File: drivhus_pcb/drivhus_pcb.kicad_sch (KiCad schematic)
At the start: 13 parts, among them J1 Setup, J10 RS-485 Right Bus, J2 Conn_01x19_Female, J3 Conn_01x19_Female, J4 RS-485 Left Bus, J5 Conn_Coaxial_Power, J6 +12V, J7 -12V, J8 +5V, J9 -5V, U1 SP3485EN

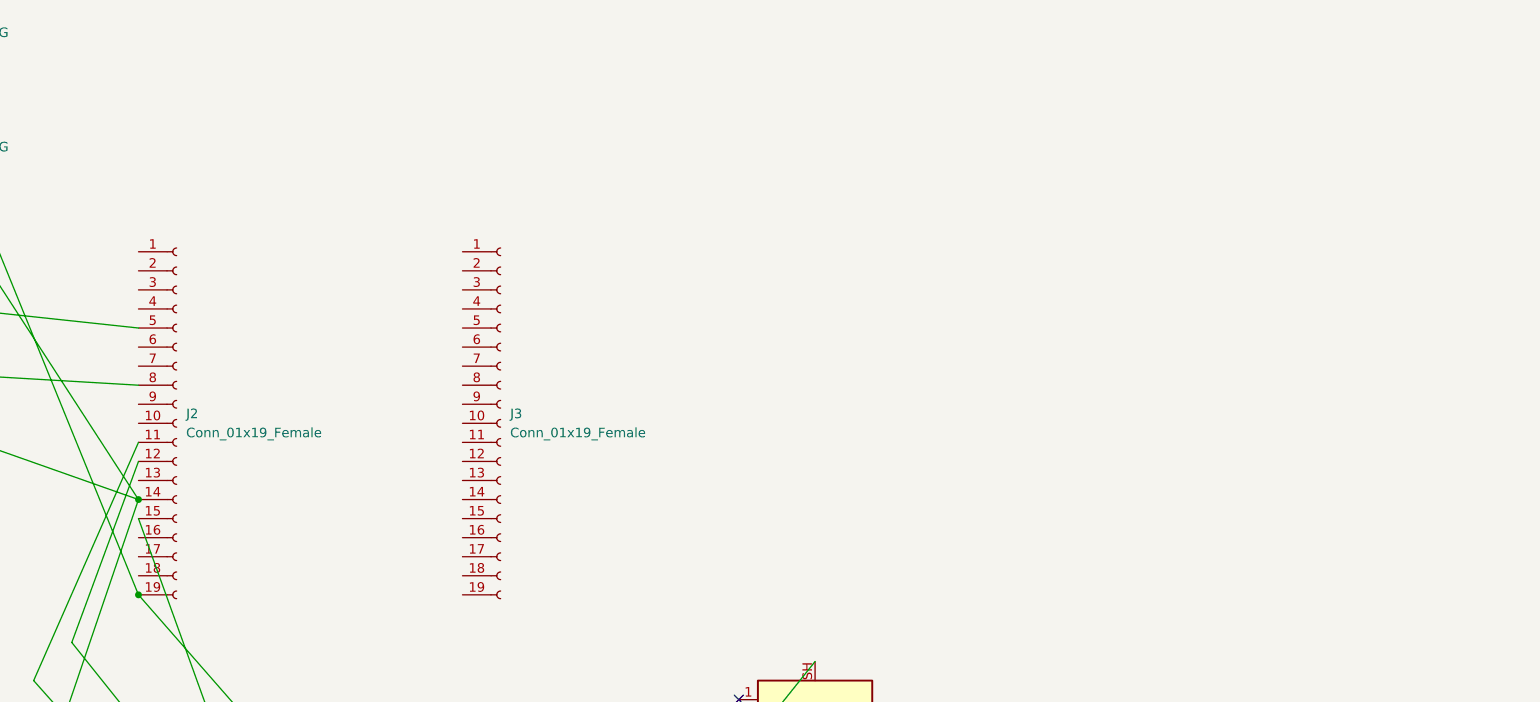
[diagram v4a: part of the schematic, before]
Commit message: Added connectors for indoor and outdoor temp/humid/light sensors
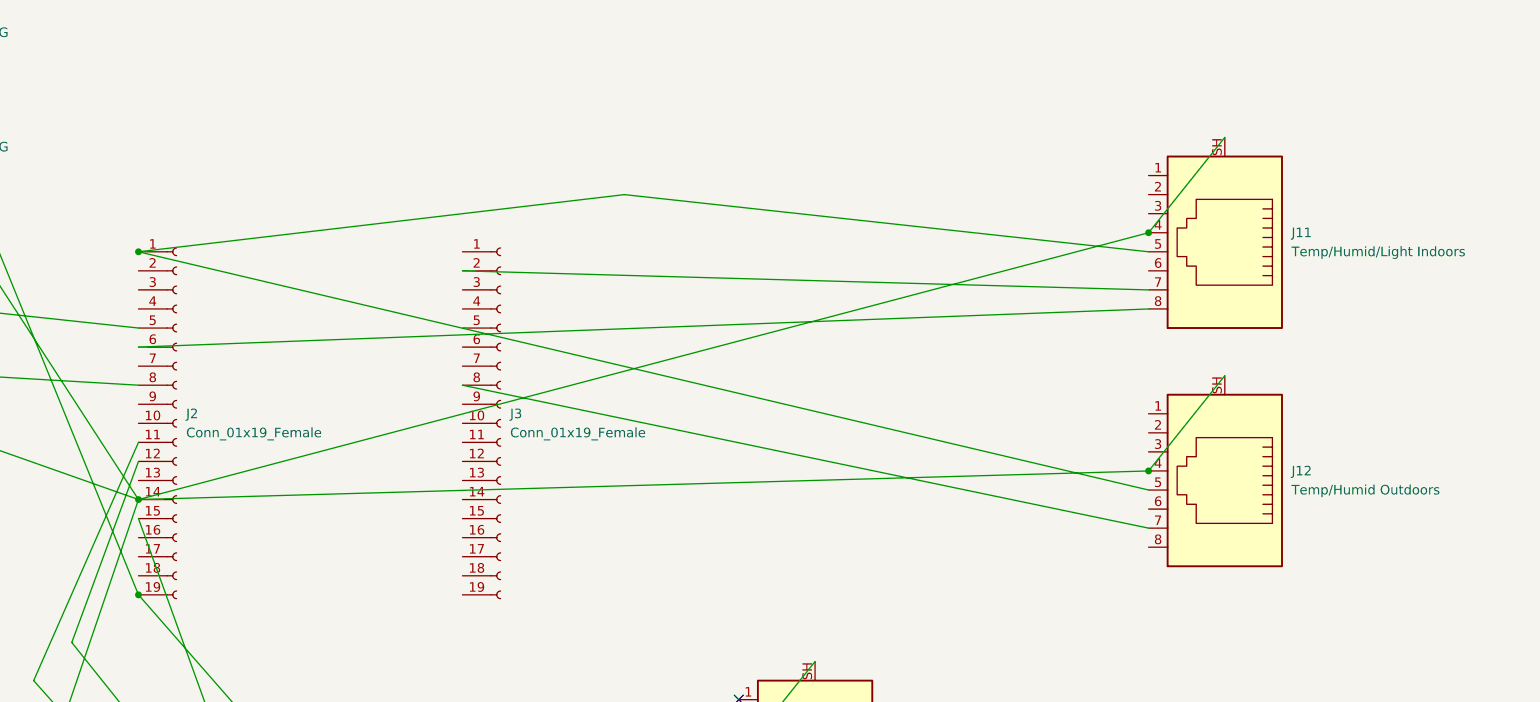
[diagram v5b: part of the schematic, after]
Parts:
- added J11: Temp/Humid/Light Indoors, Connector_RJ:RJ45_Ninigi_GE, symbol Connector:RJ45_Shielded
- added J12: Temp/Humid Outdoors, Connector_RJ:RJ45_Ninigi_GE, symbol Connector:RJ45_Shielded
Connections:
- net GND: now also J11.4, J11.SH, J12.4, J12.SH
- net at J2.1 (Pin_1): now also J11.5, J12.5
- net at J2.6 (Pin_6): now also J11.8
- net at J3.2 (Pin_2): now also J11.7
- net at J3.8 (Pin_8): now also J12.7
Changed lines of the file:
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@@
   (junction (at 99.06 107.95) (diameter 0) (color 0 0 0 0)
   )
+  (junction (at 233.68 91.44) (diameter 0) (color 0 0 0 0)
+  )
   (junction (at 27.94 64.77) (diameter 0) (color 0 0 0 0)
   )
+  (junction (at 99.06 62.23) (diameter 0) (color 0 0 0 0)
+  )
   (junction (at 135.89 146.05) (diameter 0) (color 0 0 0 0)
+  )
+  (junction (at 233.68 59.69) (diameter 0) (color 0 0 0 0)
   )
   (junction (at 68.58 33.02) (diameter 0) (color 0 0 0 0)
@@
     (stroke (width 0) (type default) (color 0 0 0 0))
   )
+  (wire (pts (xy 99.06 95.25) (xy 233.68 91.44))
+    (stroke (width 0) (type default) (color 0 0 0 0))
+  )
+  (wire (pts (xy 163.83 54.61) (xy 233.68 62.23))
+    (stroke (width 0) (type default) (color 0 0 0 0))
+  )
+  (wire (pts (xy 99.06 74.93) (xy 233.68 69.85))
+    (stroke (width 0) (type default) (color 0 0 0 0))
+  )
   (wire (pts (xy 179.07 129.54) (xy 189.23 116.84))
     (stroke (width 0) (type default) (color 0 0 0 0))
@@
     (stroke (width 0) (type default) (color 0 0 0 0))
   )
+  (wire (pts (xy 99.06 62.23) (xy 163.83 54.61))
+    (stroke (width 0) (type default) (color 0 0 0 0))
+  )
   (wire (pts (xy 115.57 146.05) (xy 115.57 151.13))
     (stroke (width 0) (type default) (color 0 0 0 0))
@@
     (stroke (width 0) (type default) (color 0 0 0 0))
   )
+  (wire (pts (xy 233.68 59.69) (xy 243.84 46.99))
+    (stroke (width 0) (type default) (color 0 0 0 0))
+  )
+  (wire (pts (xy 233.68 91.44) (xy 243.84 78.74))
+    (stroke (width 0) (type default) (color 0 0 0 0))
+  )
   (wire (pts (xy 135.89 146.05) (xy 179.07 137.16))
     (stroke (width 0) (type default) (color 0 0 0 0))
@@
     (stroke (width 0) (type default) (color 0 0 0 0))
   )
+  (wire (pts (xy 142.24 80.01) (xy 233.68 99.06))
+    (stroke (width 0) (type default) (color 0 0 0 0))
+  )
+  (wire (pts (xy 99.06 95.25) (xy 233.68 59.69))
+    (stroke (width 0) (type default) (color 0 0 0 0))
+  )
   (wire (pts (xy 99.06 95.25) (xy 78.74 154.94))
     (stroke (width 0) (type default) (color 0 0 0 0))
@@
     (stroke (width 0) (type default) (color 0 0 0 0))
   )
+  (wire (pts (xy 99.06 62.23) (xy 233.68 93.98))
+    (stroke (width 0) (type default) (color 0 0 0 0))
+  )
   (wire (pts (xy 44.45 45.72) (xy 44.45 48.26))
     (stroke (width 0) (type default) (color 0 0 0 0))
@@
     (stroke (width 0) (type default) (color 0 0 0 0))
   )
+  (wire (pts (xy 142.24 64.77) (xy 233.68 67.31))
+    (stroke (width 0) (type default) (color 0 0 0 0))
+  )
   (wire (pts (xy 125.73 138.43) (xy 179.07 132.08))
     (stroke (width 0) (type default) (color 0 0 0 0))
@@
     )
     (pin "1")
+  )
+  (symbol (lib_id "Connector:RJ45_Shielded") (at 243.84 91.44 180) (unit 1)
+    (in_bom yes) (on_board yes) (fields_autoplaced)
+    (property "Reference" "J12" (id 0) (at 252.73 91.4399 0)
+      (effects (font (size 1.27 1.27)) (justify right))
+    )
+    (property "Value" "Temp/Humid Outdoors" (id 1) (at 252.73 93.9799 0)
+      (effects (font (size 1.27 1.27)) (justify right))
+    )
+    (property "Footprint" "Connector_RJ:RJ45_Ninigi_GE" (id 2) (at 243.84 92.075 90)
+      (effects (font (size 1.27 1.27)) hide)
+    )
+    (property "Datasheet" "~" (id 3) (at 243.84 92.075 90)
+      (effects (font (size 1.27 1.27)) hide)
+    )
+    (pin "1")
+    (pin "2")
+    (pin "3")
+    (pin "4")
+    (pin "5")
+    (pin "6")
+    (pin "7")
+    (pin "8")
+    (pin "SH")
   )
   (symbol (lib_id "Connector:Conn_01x19_Female") (at 104.14 85.09 0) (unit 1)
@@
     (pin "9")
   )
+  (symbol (lib_id "Connector:RJ45_Shielded") (at 243.84 59.69 180) (unit 1)
+    (in_bom yes) (on_board yes) (fields_autoplaced)
+    (property "Reference" "J11" (id 0) (at 252.73 59.6899 0)
+      (effects (font (size 1.27 1.27)) (justify right))
+    )
+    (property "Value" "Temp/Humid/Light Indoors" (id 1) (at 252.73 62.2299 0)
+      (effects (font (size 1.27 1.27)) (justify right))
+    )
+    (property "Footprint" "Connector_RJ:RJ45_Ninigi_GE" (id 2) (at 243.84 60.325 90)
+      (effects (font (size 1.27 1.27)) hide)
+    )
+    (property "Datasheet" "~" (id 3) (at 243.84 60.325 90)
+      (effects (font (size 1.27 1.27)) hide)
+    )
+    (pin "1")
+    (pin "2")
+    (pin "3")
+    (pin "4")
+    (pin "5")
+    (pin "6")
+    (pin "7")
+    (pin "8")
+    (pin "SH")
+  )
   (symbol (lib_id "power:+5V") (at 68.58 33.02 270) (unit 1)
     (in_bom yes) (on_board yes) (fields_autoplaced)
@@
       (reference "J10") (unit 1) (value "RS-485 Right Bus") (footprint "Connector_RJ:RJ45_Ninigi_GE")
     )
+    (path "/4c469707-9012-4c4e-9b88-e445c5c64803"
+      (reference "J11") (unit 1) (value "Temp/Humid/Light Indoors") (footprint "Connector_RJ:RJ45_Ninigi_GE")
+    )
+    (path "/1a8cb90e-f5bd-4cd7-b987-feae025c484b"
+      (reference "J12") (unit 1) (value "Temp/Humid Outdoors") (footprint "Connector_RJ:RJ45_Ninigi_GE")
+    )
     (path "/57442f99-2d46-4e71-bd92-43296b060c85"

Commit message: Added relays. Added lots and lots of relays...
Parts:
- added D1, D10, D11, D12, D13, D14, D15, D2, D3, D4, D5, D6, D7, D8, D9: D, Diode_SMD:D_SMB, symbol Device:D
- added J13, J14, J15, J16, J17, J18, J19, J20, J21, J22, J23, J24, J25, J26, J27: Conn_01x02_Male, TerminalBlock:TerminalBlock_bornier-2_P5.08mm, symbol Connector:Conn_01x02_Male
- added K1, K10, K11, K12, K13, K14, K15, K2, K3, K4, K5, K6, K7, K8, K9: SANYOU_SRD_Form_C, Relay_THT:Relay_SPDT_SANYOU_SRD_Series_Form_C, symbol Relay:SANYOU_SRD_Form_C
- added Q1, Q10, Q11, Q12, Q13, Q14, Q15, Q2, Q3, Q4, Q5, Q6, Q7, Q8, Q9: BC817, Package_TO_SOT_SMD:SOT-23, symbol Transistor_BJT:BC817
- added R10, R11, R12, R13, R14, R15, R16, R17, R3, R4, R5, R6, R7, R8, R9: 1K, Resistor_SMD:R_1206_3216Metric, symbol Device:R
- added U2: CD74HC4067M, Package_SO:SOIC-24W_7.5x15.4mm_P1.27mm, symbol 74xx:CD74HC4067M
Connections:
- net +5V: now also D1.1 (K), D10.1 (K), D11.1 (K), D12.1 (K), D13.1 (K), D14.1 (K), D15.1 (K), D2.1 (K), D3.1 (K), D4.1 (K), D5.1 (K), D6.1 (K), D7.1 (K), D8.1 (K), D9.1 (K), K1.5, K10.5, K11.5, K12.5, K13.5, K14.5, K15.5, K2.5, K3.5, K4.5, K5.5, K6.5, K7.5, K8.5, K9.5, U2.24 (VCC)
- net GND: now also Q1.2 (E), Q10.2 (E), Q11.2 (E), Q12.2 (E), Q13.2 (E), Q14.2 (E), Q15.2 (E), Q2.2 (E), Q3.2 (E), Q4.2 (E), Q5.2 (E), Q6.2 (E), Q7.2 (E), Q8.2 (E), Q9.2 (E), U2.12 (GND), U2.15 (~{E})
- net at J2.10 (Pin_10): now also U2.10 (S0)
- net at J2.7 (Pin_7): now also U2.1 (COM)
- net at J2.9 (Pin_9): now also U2.11 (S1)
- net +12V: now reaches J5.1 (In), J6.1 (Pin_1), J6.2 (Pin_2), R1.1
- net +12V: now also K1.1, K10.1, K11.1, K12.1, K13.1, K14.1, K15.1, K2.1, K3.1, K4.1, K5.1, K6.1, K7.1, K8.1, K9.1
- net -12V: now reaches J5.2 (Ext), J7.1 (Pin_1), J7.2 (Pin_2), R2.2
- net -12V: now also J13.1 (Pin_1), J14.1 (Pin_1), J15.1 (Pin_1), J16.1 (Pin_1), J17.1 (Pin_1), J18.1 (Pin_1), J19.1 (Pin_1), J20.1 (Pin_1), J21.1 (Pin_1), J22.1 (Pin_1), J23.1 (Pin_1), J24.1 (Pin_1), J25.1 (Pin_1), J26.1 (Pin_1), J27.1 (Pin_1)
- net at J3.10 (Pin_10): now also U2.13 (S3)
- net at J3.9 (Pin_9): now also U2.14 (S2)
- new net: Q12.1 (B), R14.2
- new net: D12.2 (A), K12.2, Q12.3 (C)
- new net: Q9.1 (B), R11.2
- new net: D9.2 (A), K9.2, Q9.3 (C)
- new net: J16.2 (Pin_2), K4.3
- new net: D8.2 (A), K8.2, Q8.3 (C)
- new net: J24.2 (Pin_2), K12.3
- new net: Q2.1 (B), R4.2
- new net: D2.2 (A), K2.2, Q2.3 (C)
- new net: J27.2 (Pin_2), K15.3
- new net: D4.2 (A), K4.2, Q4.3 (C)
- new net: D6.2 (A), K6.2, Q6.3 (C)
- new net: D10.2 (A), K10.2, Q10.3 (C)
- new net: J22.2 (Pin_2), K10.3
- new net: J19.2 (Pin_2), K7.3
- new net: R4.1, U2.7 (I2)
- new net: J18.2 (Pin_2), K6.3
- new net: Q11.1 (B), R13.2
- new net: D11.2 (A), K11.2, Q11.3 (C)
- new net: R7.1, U2.4 (I5)
- new net: Q5.1 (B), R7.2
- new net: D15.2 (A), K15.2, Q15.3 (C)
- new net: R13.1, U2.20 (I11)
- new net: R3.1, U2.8 (I1)
- new net: Q1.1 (B), R3.2
- new net: R10.1, U2.23 (I8)
- new net: Q8.1 (B), R10.2
- new net: D1.2 (A), K1.2, Q1.3 (C)
- new net: D3.2 (A), K3.2, Q3.3 (C)
- new net: Q10.1 (B), R12.2
- new net: J26.2 (Pin_2), K14.3
- new net: D13.2 (A), K13.2, Q13.3 (C)
- new net: J13.2 (Pin_2), K1.3
- new net: Q3.1 (B), R5.2
- new net: Q4.1 (B), R6.2
- new net: R9.1, U2.2 (I7)
- new net: Q7.1 (B), R9.2
- new net: J14.2 (Pin_2), K2.3
- new net: D5.2 (A), K5.2, Q5.3 (C)
- new net: J17.2 (Pin_2), K5.3
- new net: R11.1, U2.22 (I9)
- new net: R17.1, U2.16 (I15)
- new net: R16.1, U2.17 (I14)
- new net: R15.1, U2.18 (I13)
- new net: R14.1, U2.19 (I12)
- new net: R12.1, U2.21 (I10)
- new net: R8.1, U2.3 (I6)
- new net: R6.1, U2.5 (I4)
- new net: R5.1, U2.6 (I3)
- new net: J15.2 (Pin_2), K3.3
- new net: Q15.1 (B), R17.2
- new net: J20.2 (Pin_2), K8.3
- new net: Q13.1 (B), R15.2
- new net: J25.2 (Pin_2), K13.3
- new net: J21.2 (Pin_2), K9.3
- new net: J23.2 (Pin_2), K11.3
- new net: Q6.1 (B), R8.2
- new net: D7.2 (A), K7.2, Q7.3 (C)
- new net: Q14.1 (B), R16.2
- new net: D14.2 (A), K14.2, Q14.3 (C)
- no-connect marks 8 -> 33
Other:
- moved on the sheet: J1, J10, J11, J12, J2, J3, J4, J5, J6, J7, J8, J9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

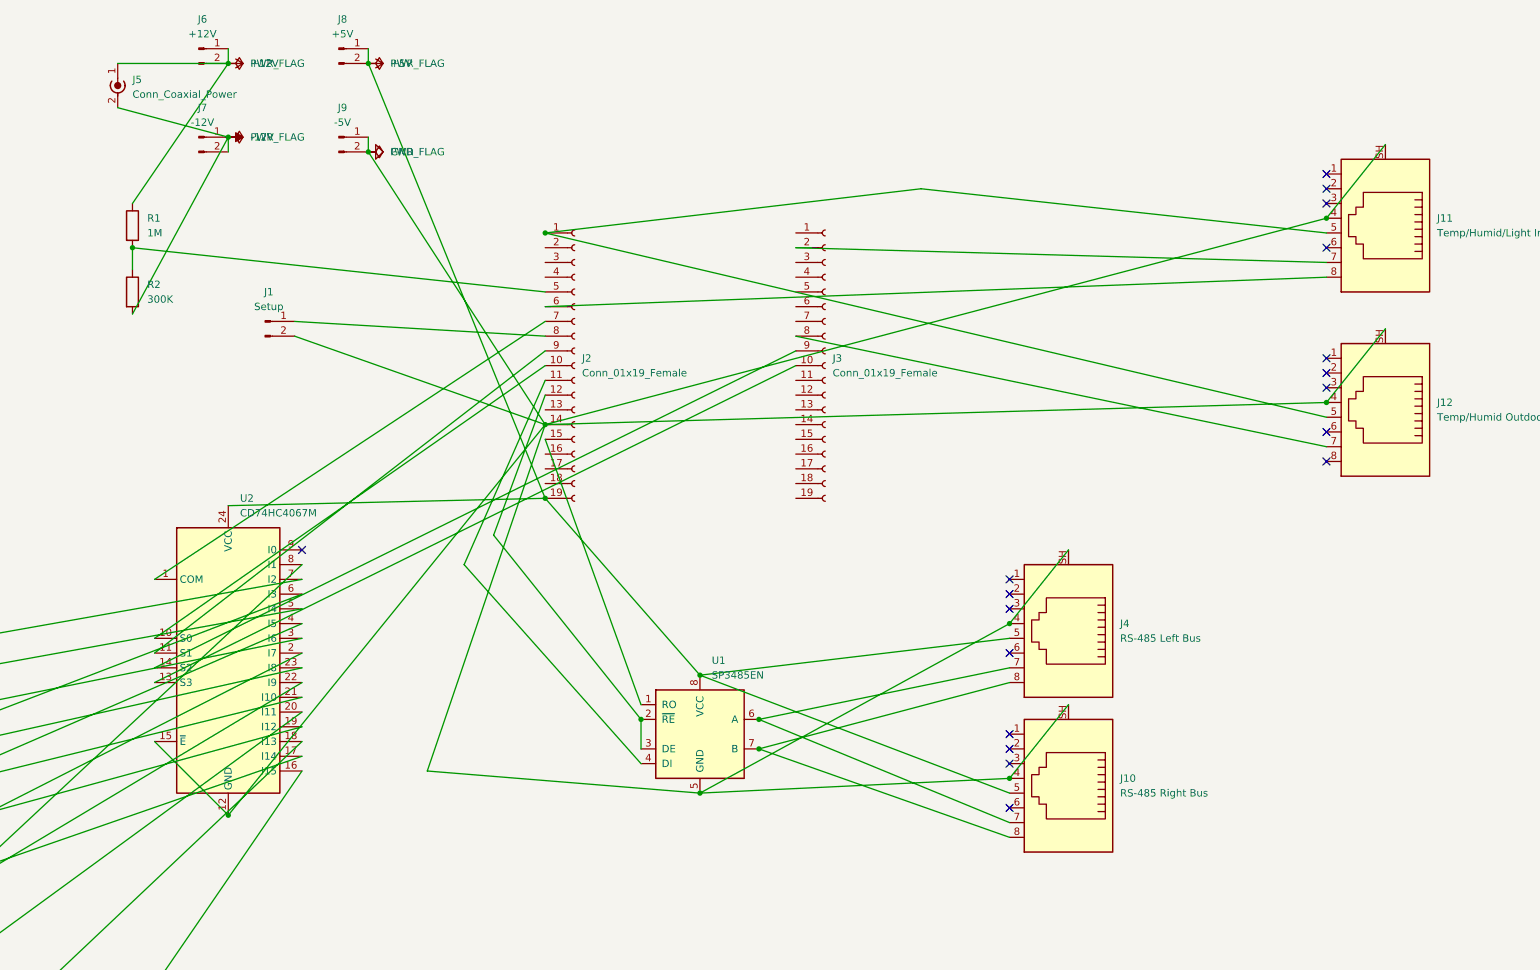
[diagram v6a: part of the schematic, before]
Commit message: Cleaned up the schematic power lines
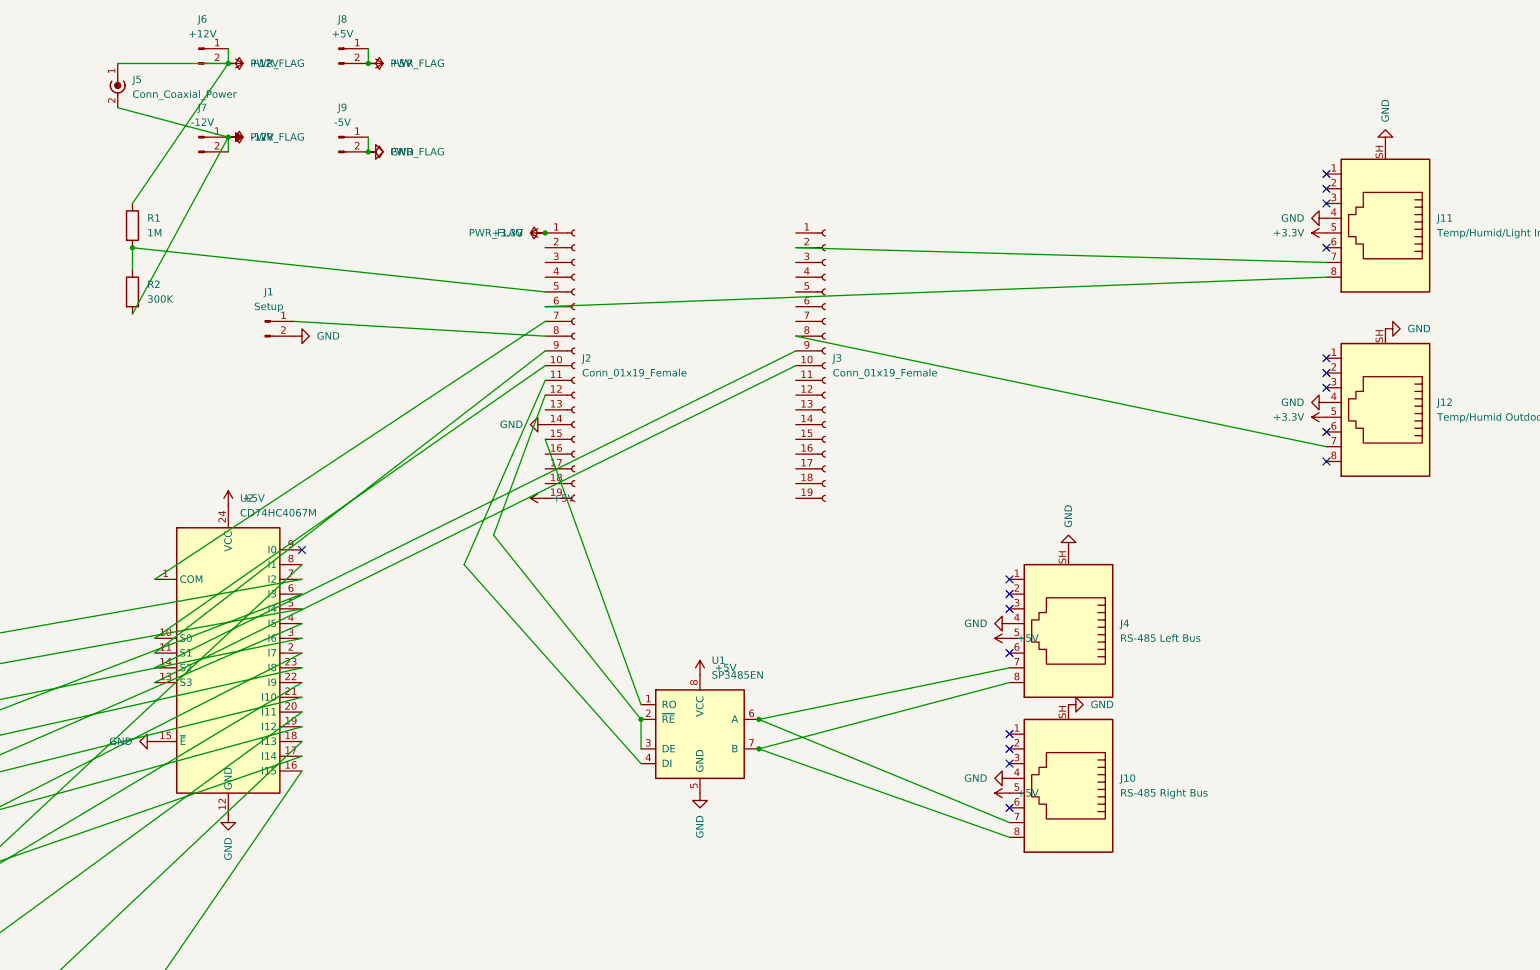
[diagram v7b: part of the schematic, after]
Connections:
- net +3.3V: now reaches J11.5, J12.5, J2.1 (Pin_1)

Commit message: Added connector for pumps
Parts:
- removed J13, J14, J15, J16, J17, J18, J19, J20, J21, J22, J23, J24, J25, J26, J27: Conn_01x02_Male, TerminalBlock:TerminalBlock_bornier-2_P5.08mm, symbol Connector:Conn_01x02_Male
- added J13: Pump 1-4, Connector_RJ:RJ45_Ninigi_GE, symbol Connector:RJ45_Shielded
- added J14: Pump 5-8, Connector_RJ:RJ45_Ninigi_GE, symbol Connector:RJ45_Shielded
- added J15: Pump 9-12, Connector_RJ:RJ45_Ninigi_GE, symbol Connector:RJ45_Shielded
- added J16: Pump 13-15, Connector_RJ:RJ45_Ninigi_GE, symbol Connector:RJ45_Shielded
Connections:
- net -12V: now also J13.1, J13.2, J13.3, J13.6, J13.SH, J14.1, J14.2, J14.3, J14.6, J14.SH, J15.1, J15.2, J15.3, J15.6, J15.SH, J16.1, J16.2, J16.3, J16.6, J16.SH
- net at K4.3: now also J13.8
- net at K12.3: now also J15.8
- net at K15.3: now also J16.7
- net at K10.3: now also J15.5
- net at K7.3: now also J14.7
- net at K6.3: now also J14.5
- net at K14.3: now also J16.5
- net at K1.3: now also J13.4
- net at K2.3: now also J13.5
- net at K5.3: now also J14.4
- net at K3.3: now also J13.7
- net at K8.3: now also J14.8
- net at K13.3: now also J16.4
- net at K9.3: now also J15.4
- net at K11.3: now also J15.7
- no-connect marks 33 -> 34
